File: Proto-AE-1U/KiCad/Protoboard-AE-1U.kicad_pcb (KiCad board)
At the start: 2 copper layers, 1 part

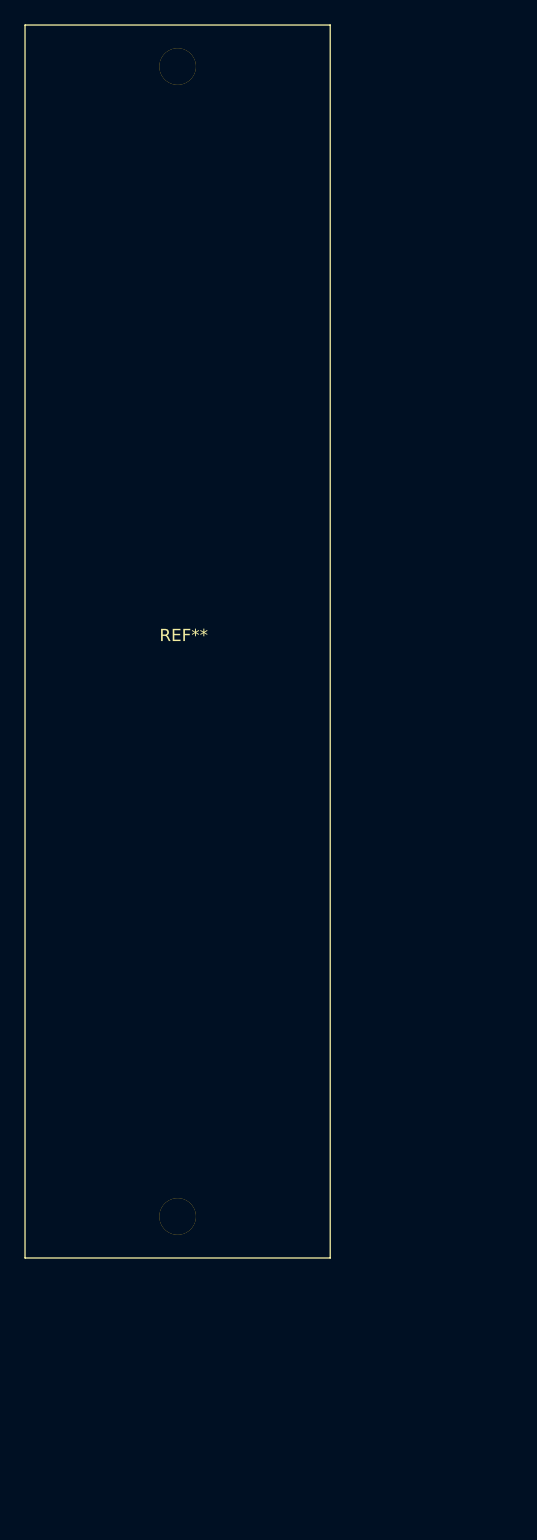
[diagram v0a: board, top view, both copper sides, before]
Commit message: created AE-1U-Protoboard
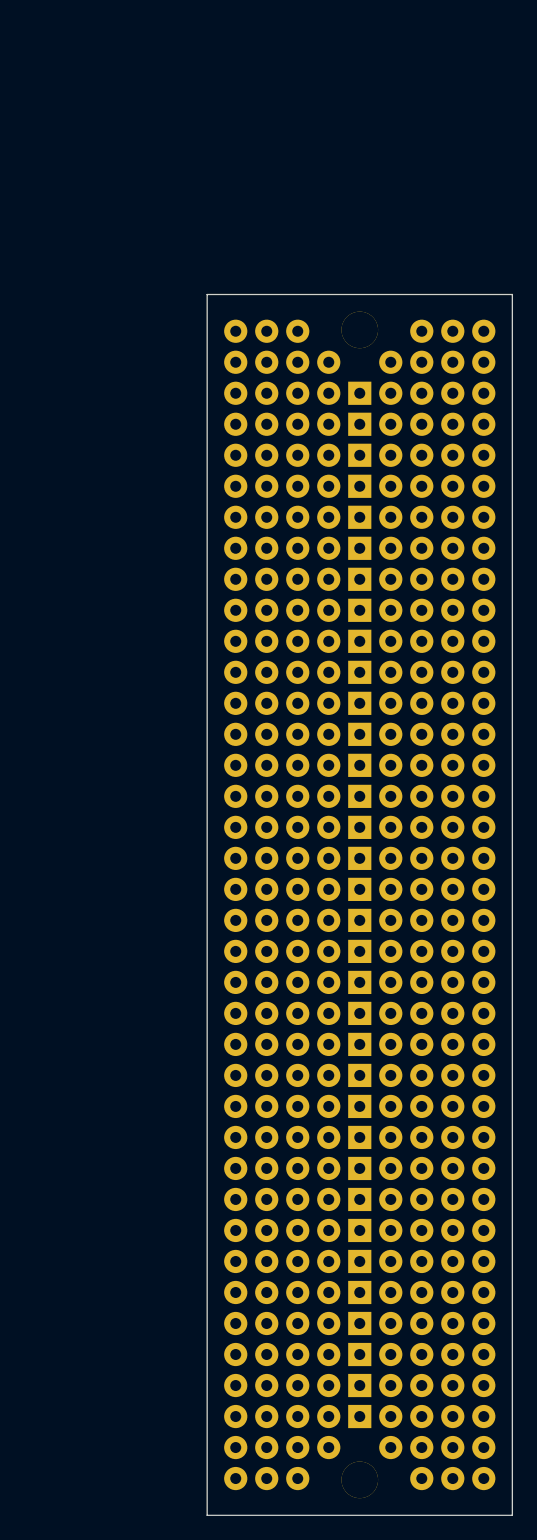
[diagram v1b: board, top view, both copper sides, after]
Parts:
- removed the REF** at (89.0, 131.0)
- added REF**: Pad, clectric-diy:Pad, F.Cu at (106.3, 72.9)
- added REF**: Pad, clectric-diy:Pad, F.Cu at (106.3, 105.9)
- added REF**: Pad, clectric-diy:Pad, F.Cu at (124.0, 65.2)
- added REF**: Pad, clectric-diy:Pad, F.Cu at (113.9, 121.1)
- added REF**: Pad, clectric-diy:Pad, F.Cu at (124.0, 80.5)
- added REF**: Pad, clectric-diy:Pad, F.Cu at (113.9, 88.1)
- added REF**: Pad, clectric-diy:Pad, F.Cu at (121.5, 149.1)
- added REF**: Pad, clectric-diy:Pad, F.Cu at (111.3, 131.3)
- added REF**: Pad, clectric-diy:Pad, F.Cu at (121.5, 133.8)
- added REF**: Pad, clectric-diy:Pad, F.Cu at (108.8, 62.7)
- added REF**: Pad, clectric-diy:Pad, F.Cu at (113.9, 113.5)
- added REF**: Pad, clectric-diy:Pad, F.Cu at (119.0, 113.5)
- added REF**: Pad, clectric-diy:Pad, F.Cu at (106.3, 138.9)
- added REF**: Pad, clectric-diy:Pad, F.Cu at (124.0, 75.4)
- added REF**: Pad, clectric-diy:Pad, F.Cu at (116.4, 123.7)
- added REF**: Pad, clectric-diy:Pad, F.Cu at (108.8, 108.4)
- added REF**: Pad, clectric-diy:Pad, F.Cu at (116.4, 67.8)
- added REF**: Pad, clectric-diy:Pad, F.Cu at (111.3, 80.5)
- added REF**: Pad, clectric-diy:Pad, F.Cu at (116.4, 111.0)
- added REF**: Pad, clectric-diy:Pad, F.Cu at (126.6, 75.4)
- added REF**: Pad, clectric-diy:Pad, F.Cu at (121.5, 116.0)
- added REF**: Pad, clectric-diy:Pad, F.Cu at (108.8, 116.0)
- added REF**: Pad, clectric-diy:Pad, F.Cu at (111.3, 136.4)
- added REF**: Pad, clectric-diy:Pad, F.Cu at (106.3, 95.7)
- added REF**: Pad, clectric-diy:Pad, F.Cu at (121.5, 126.2)
- added REF**: Pad, clectric-diy:Pad, F.Cu at (108.8, 149.1)
- added REF**: Pad, clectric-diy:Pad, F.Cu at (116.4, 121.1)
- added REF**: Pad, clectric-diy:Pad, F.Cu at (108.8, 136.4)
- added REF**: Pad, clectric-diy:Pad, F.Cu at (119.0, 60.2)
- added REF**: Pad, clectric-diy:Pad, F.Cu at (121.5, 67.8)
- added REF**: Pad, clectric-diy:Pad, F.Cu at (121.5, 90.6)
- added REF**: Pad, clectric-diy:Pad, F.Cu at (124.0, 105.9)
- added REF**: Pad, clectric-diy:Pad, F.Cu at (116.4, 80.5)
- added REF**: Pad, clectric-diy:Pad, F.Cu at (106.3, 108.4)
- added REF**: Pad, clectric-diy:Pad, F.Cu at (106.3, 85.6)
- added REF**: Pad, clectric-diy:Pad, F.Cu at (108.8, 90.6)
- added REF**: Pad, clectric-diy:Pad, F.Cu at (121.5, 98.3)
- added REF**: Pad, clectric-diy:Pad, F.Cu at (116.4, 75.4)
- added REF**: Pad, clectric-diy:Pad, F.Cu at (119.0, 103.3)
- added REF**: Pad, clectric-diy:Pad, F.Cu at (121.5, 108.4)
- added REF**: Pad, clectric-diy:Pad, F.Cu at (108.8, 133.8)
- added REF**: Pad, clectric-diy:Pad, F.Cu at (111.3, 77.9)
- added REF**: Pad, clectric-diy:Pad, F.Cu at (111.3, 100.8)
- added REF**: Pad, clectric-diy:Pad, F.Cu at (119.0, 105.9)
- added REF**: Pad, clectric-diy:Pad, F.Cu at (126.6, 121.1)
- added REF**: Pad, clectric-diy:Pad, F.Cu at (116.4, 118.6)
- added REF**: Pad, clectric-diy:Pad, F.Cu at (126.6, 136.4)
- added REF**: Pad, clectric-diy:Pad, F.Cu at (121.5, 141.4)
- added REF**: Pad, clectric-diy:Pad, F.Cu at (116.4, 116.0)
- added REF**: Pad, clectric-diy:Pad, F.Cu at (111.3, 123.7)
- added REF**: Pad, clectric-diy:Pad, F.Cu at (121.5, 121.1)
- added REF**: Pad, clectric-diy:Pad, F.Cu at (108.8, 111.0)
- added REF**: Pad, clectric-diy:Pad, F.Cu at (108.8, 88.1)
- added REF**: Pad, clectric-diy:Pad, F.Cu at (106.3, 116.0)
- added REF**: Pad, clectric-diy:Pad, F.Cu at (111.3, 65.2)
- added REF**: Pad, clectric-diy:Pad, F.Cu at (119.0, 75.4)
- added REF**: Pad, clectric-diy:Pad, F.Cu at (119.0, 146.5)
- added REF**: Pad, clectric-diy:Pad, F.Cu at (124.0, 100.8)
- added REF**: Pad, clectric-diy:Pad, F.Cu at (106.3, 80.5)
- added REF**: Pad, clectric-diy:Pad, F.Cu at (119.0, 90.6)
- added REF**: Pad, clectric-diy:Pad, F.Cu at (121.5, 144.0)
- added REF**: Pad, clectric-diy:Pad, F.Cu at (111.3, 108.4)
- added REF**: Pad, clectric-diy:Pad, F.Cu at (111.3, 72.9)
- added REF**: Pad, clectric-diy:Pad, F.Cu at (126.6, 144.0)
- added REF**: Pad, clectric-diy:Pad, F.Cu at (116.4, 133.8)
- added REF**: Pad, clectric-diy:Pad, F.Cu at (113.9, 133.8)
- added REF**: Pad, clectric-diy:Pad, F.Cu at (108.8, 93.2)
- added REF**: Pad, clectric-diy:Pad, F.Cu at (113.9, 141.4)
- added REF**: Pad, clectric-diy:Pad, F.Cu at (121.5, 72.9)
- added REF**: Pad, clectric-diy:Pad, F.Cu at (119.0, 133.8)
- added REF**: Pad, clectric-diy:Pad, F.Cu at (113.9, 123.7)
- added REF**: Pad, clectric-diy:Pad, F.Cu at (106.3, 90.6)
- added REF**: Pad, clectric-diy:Pad, F.Cu at (111.3, 55.1)
- added REF**: Pad, clectric-diy:Pad, F.Cu at (113.9, 93.2)
- added REF**: Pad, clectric-diy:Pad, F.Cu at (113.9, 67.8)
- added REF**: Pad, clectric-diy:Pad, F.Cu at (108.8, 146.5)
- added REF**: Pad, clectric-diy:Pad, F.Cu at (111.3, 118.6)
- added REF**: Pad, clectric-diy:Pad, F.Cu at (111.3, 85.6)
- added REF**: Pad, clectric-diy:Pad, F.Cu at (113.9, 103.3)
- added REF**: Pad, clectric-diy:Pad, F.Cu at (113.9, 77.9)
- added REF**: Pad, clectric-diy:Pad, F.Cu at (108.8, 131.3)
- added REF**: Pad, clectric-diy:Pad, F.Cu at (111.3, 98.3)
- added REF**: Pad, clectric-diy:Pad, F.Cu at (121.5, 83.0)
- added REF**: Pad, clectric-diy:Pad, F.Cu at (116.4, 65.2)
- added REF**: Pad, clectric-diy:Pad, F.Cu at (113.9, 100.8)
- added REF**: Pad, clectric-diy:Pad, F.Cu at (121.5, 85.6)
- added REF**: Pad, clectric-diy:Pad, F.Cu at (106.3, 111.0)
- added REF**: Pad, clectric-diy:Pad, F.Cu at (111.3, 93.2)
- added REF**: Pad, clectric-diy:Pad, F.Cu at (113.9, 98.3)
- added REF**: Pad, clectric-diy:Pad, F.Cu at (111.3, 95.7)
- added REF**: Pad, clectric-diy:Pad, F.Cu at (119.0, 144.0)
- added REF**: Pad, clectric-diy:Pad, F.Cu at (124.0, 126.2)
- added REF**: Pad, clectric-diy:Pad, F.Cu at (106.3, 126.2)
- added REF**: Pad, clectric-diy:Pad, F.Cu at (116.4, 136.4)
- added REF**: Pad, clectric-diy:Pad, F.Cu at (108.8, 123.7)
- added REF**: Pad, clectric-diy:Pad, F.Cu at (116.4, 131.3)
- added REF**: Pad, clectric-diy:Pad, F.Cu at (124.0, 116.0)
- added REF**: Pad, clectric-diy:Pad, F.Cu at (121.5, 128.7)
- added REF**: Pad, clectric-diy:Pad, F.Cu at (111.3, 126.2)
- added REF**: Pad, clectric-diy:Pad, F.Cu at (116.4, 93.2)
- added REF**: Pad, clectric-diy:Pad, F.Cu at (121.5, 55.1)
- added REF**: Pad, clectric-diy:Pad, F.Cu at (106.3, 100.8)
- added REF**: Pad, clectric-diy:Pad, F.Cu at (116.4, 144.0)
- added REF**: Pad, clectric-diy:Pad, F.Cu at (108.8, 72.9)
- added REF**: Pad, clectric-diy:Pad, F.Cu at (111.3, 90.6)
- added REF**: Pad, clectric-diy:Pad, F.Cu at (108.8, 98.3)
- added REF**: Pad, clectric-diy:Pad, F.Cu at (124.0, 118.6)
- added REF**: Pad, clectric-diy:Pad, F.Cu at (119.0, 126.2)
- added REF**: Pad, clectric-diy:Pad, F.Cu at (106.3, 123.7)
- added REF**: Pad, clectric-diy:Pad, F.Cu at (108.8, 77.9)
- added REF**: Pad, clectric-diy:Pad, F.Cu at (106.3, 55.1)
- added REF**: Pad, clectric-diy:Pad, F.Cu at (113.9, 90.6)
- added REF**: Pad, clectric-diy:Pad, F.Cu at (106.3, 144.0)
- added REF**: Pad, clectric-diy:Pad, F.Cu at (126.6, 62.7)
- added REF**: Pad, clectric-diy:Pad, F.Cu at (119.0, 93.2)
- added REF**: Pad, clectric-diy:Pad, F.Cu at (126.6, 65.2)
- added REF**: Pad, clectric-diy:Pad, F.Cu at (111.3, 67.8)
- added REF**: Pad, clectric-diy:Pad, F.Cu at (108.8, 126.2)
- added REF**: Pad, clectric-diy:Pad, F.Cu at (124.0, 77.9)
- added REF**: Pad, clectric-diy:Pad, F.Cu at (106.3, 118.6)
- added REF**: Pad, clectric-diy:Pad, F.Cu at (108.8, 128.7)
- added REF**: Pad, clectric-diy:Pad, F.Cu at (126.6, 77.9)
- added REF**: Pad, clectric-diy:Pad, F.Cu at (126.6, 141.4)
- added REF**: Pad, clectric-diy:Pad, F.Cu at (108.8, 60.2)
- added REF**: Pad, clectric-diy:Pad, F.Cu at (119.0, 80.5)
- added REF**: Pad, clectric-diy:Pad, F.Cu at (124.0, 57.6)
- added REF**: Pad, clectric-diy:Pad, F.Cu at (116.4, 88.1)
- added REF**: Pad, clectric-diy:Pad, F.Cu at (119.0, 108.4)
- added REF**: Pad, clectric-diy:Pad, F.Cu at (119.0, 138.9)
- added REF**: Pad, clectric-diy:Pad, F.Cu at (119.0, 65.2)
- added REF**: Pad, clectric-diy:Pad, F.Cu at (126.6, 146.5)
- added REF**: Pad, clectric-diy:Pad, F.Cu at (126.6, 118.6)
- added REF**: Pad, clectric-diy:Pad, F.Cu at (111.3, 138.9)
- added REF**: Pad, clectric-diy:Pad, F.Cu at (111.3, 105.9)
- added REF**: Pad, clectric-diy:Pad, F.Cu at (111.3, 149.1)
- added REF**: Pad, clectric-diy:Pad, F.Cu at (106.3, 77.9)
- added REF**: Pad, clectric-diy:Pad, F.Cu at (113.9, 118.6)
- added REF**: Pad, clectric-diy:Pad, F.Cu at (121.5, 95.7)
- added REF**: Pad, clectric-diy:Pad, F.Cu at (113.9, 128.7)
- added REF**: Pad, clectric-diy:Pad, F.Cu at (108.8, 67.8)
- added REF**: Pad, clectric-diy:Pad, F.Cu at (121.5, 93.2)
- added REF**: Pad, clectric-diy:Pad, F.Cu at (113.9, 144.0)
- added REF**: Pad, clectric-diy:Pad, F.Cu at (119.0, 83.0)
- added REF**: Pad, clectric-diy:Pad, F.Cu at (106.3, 103.3)
- added REF**: Pad, clectric-diy:Pad, F.Cu at (126.6, 133.8)
- added REF**: Pad, clectric-diy:Pad, F.Cu at (119.0, 95.7)
- added REF**: Pad, clectric-diy:Pad, F.Cu at (106.3, 65.2)
- added REF**: Pad, clectric-diy:Pad, F.Cu at (111.3, 83.0)
- added REF**: Pad, clectric-diy:Pad, F.Cu at (116.4, 138.9)
- added REF**: Pad, clectric-diy:Pad, F.Cu at (126.6, 131.3)
- added REF**: Pad, clectric-diy:Pad, F.Cu at (121.5, 88.1)
- added REF**: Pad, clectric-diy:Pad, F.Cu at (121.5, 123.7)
- added REF**: Pad, clectric-diy:Pad, F.Cu at (121.5, 138.9)
- added REF**: Pad, clectric-diy:Pad, F.Cu at (126.6, 111.0)
- added REF**: Pad, clectric-diy:Pad, F.Cu at (108.8, 100.8)
- added REF**: Pad, clectric-diy:Pad, F.Cu at (113.9, 72.9)
- added REF**: Pad, clectric-diy:Pad, F.Cu at (126.6, 126.2)
- added REF**: Pad, clectric-diy:Pad, F.Cu at (108.8, 118.6)
- added REF**: Pad, clectric-diy:Pad, F.Cu at (126.6, 98.3)
- added REF**: Pad, clectric-diy:Pad, F.Cu at (124.0, 108.4)
- added REF**: Pad, clectric-diy:Pad, F.Cu at (111.3, 133.8)
- added REF**: Pad, clectric-diy:Pad, F.Cu at (124.0, 83.0)
- added REF**: Pad, clectric-diy:Pad, F.Cu at (108.8, 113.5)
- added REF**: Pad, clectric-diy:Pad, F.Cu at (108.8, 80.5)
- added REF**: Pad, clectric-diy:Pad, F.Cu at (119.0, 128.7)
- added REF**: Pad, clectric-diy:Pad, F.Cu at (119.0, 70.3)
- added REF**: Pad, clectric-diy:Pad, F.Cu at (126.6, 60.2)
- added REF**: Pad, clectric-diy:Pad, F.Cu at (113.9, 85.6)
- added REF**: Pad, clectric-diy:Pad, F.Cu at (106.3, 88.1)
- added REF**: Pad, clectric-diy:Pad, F.Cu at (119.0, 88.1)
- added REF**: Pad, clectric-diy:Pad, F.Cu at (113.9, 70.3)
- added REF**: Pad, clectric-diy:Pad, F.Cu at (124.0, 138.9)
- added REF**: Pad, clectric-diy:Pad, F.Cu at (106.3, 141.4)
- added REF**: Pad, clectric-diy:Pad, F.Cu at (124.0, 103.3)
- added REF**: Pad, clectric-diy:Pad, F.Cu at (121.5, 111.0)
- added REF**: Pad, clectric-diy:Pad, F.Cu at (108.8, 141.4)
- added REF**: Pad, clectric-diy:Pad, F.Cu at (119.0, 57.6)
- added REF**: Pad, clectric-diy:Pad, F.Cu at (126.6, 100.8)
- added REF**: Pad, clectric-diy:Pad, F.Cu at (116.4, 90.6)
- added REF**: Pad, clectric-diy:Pad, F.Cu at (124.0, 98.3)
- added REF**: Pad, clectric-diy:Pad, F.Cu at (126.6, 138.9)
- added REF**: Pad, clectric-diy:Pad, F.Cu at (124.0, 88.1)
- added REF**: Pad, clectric-diy:Pad, F.Cu at (108.8, 95.7)
- added REF**: Pad, clectric-diy:Pad, F.Cu at (124.0, 67.8)
- added REF**: Pad, clectric-diy:Pad, F.Cu at (119.0, 98.3)
- added REF**: Pad, clectric-diy:Pad, F.Cu at (111.3, 111.0)
- added REF**: Pad, clectric-diy:Pad, F.Cu at (126.6, 72.9)
- added REF**: Pad, clectric-diy:Pad, F.Cu at (108.8, 144.0)
- added REF**: Pad, clectric-diy:Pad, F.Cu at (116.4, 154.1)
- added REF**: Pad, clectric-diy:Pad, F.Cu at (124.0, 149.1)
- added REF**: Pad, clectric-diy:Pad, F.Cu at (124.0, 136.4)
- added REF**: Pad, clectric-diy:Pad, F.Cu at (126.6, 108.4)
- added REF**: Pad, clectric-diy:Pad, F.Cu at (106.3, 149.1)
- added REF**: Pad, clectric-diy:Pad, F.Cu at (121.5, 146.5)
- added REF**: Pad, clectric-diy:Pad, F.Cu at (116.4, 113.5)
- added REF**: Pad, clectric-diy:Pad, F.Cu at (124.0, 90.6)
- added REF**: Pad, clectric-diy:Pad, F.Cu at (126.6, 90.6)
- added REF**: Pad, clectric-diy:Pad, F.Cu at (126.6, 80.5)
- added REF**: Pad, clectric-diy:Pad, F.Cu at (119.0, 121.1)
- added REF**: Pad, clectric-diy:Pad, F.Cu at (126.6, 105.9)
- added REF**: Pad, clectric-diy:Pad, F.Cu at (106.3, 128.7)
- added REF**: Pad, clectric-diy:Pad, F.Cu at (111.3, 70.3)
- added REF**: Pad, clectric-diy:Pad, F.Cu at (111.3, 141.4)
- added REF**: Pad, clectric-diy:Pad, F.Cu at (116.4, 77.9)
- added REF**: Pad, clectric-diy:Pad, F.Cu at (124.0, 141.4)
- added REF**: Pad, clectric-diy:Pad, F.Cu at (126.6, 93.2)
- added REF**: Pad, clectric-diy:Pad, F.Cu at (126.6, 88.1)
- added REF**: Pad, clectric-diy:Pad, F.Cu at (106.3, 60.2)
- added REF**: Pad, clectric-diy:Pad, F.Cu at (126.6, 128.7)
- added REF**: Pad, clectric-diy:Pad, F.Cu at (119.0, 118.6)
- added REF**: Pad, clectric-diy:Pad, F.Cu at (119.0, 72.9)
- added REF**: Pad, clectric-diy:Pad, F.Cu at (121.5, 57.6)
- added REF**: Pad, clectric-diy:Pad, F.Cu at (106.3, 67.8)
- added REF**: Pad, clectric-diy:Pad, F.Cu at (116.4, 83.0)
- added REF**: Pad, clectric-diy:Pad, F.Cu at (126.6, 95.7)
- added REF**: Pad, clectric-diy:Pad, F.Cu at (126.6, 113.5)
- added REF**: Pad, clectric-diy:Pad, F.Cu at (124.0, 144.0)
- added REF**: Pad, clectric-diy:Pad, F.Cu at (121.5, 103.3)
- added REF**: Pad, clectric-diy:Pad, F.Cu at (124.0, 128.7)
- added REF**: Pad, clectric-diy:Pad, F.Cu at (121.5, 113.5)
- added REF**: Pad, clectric-diy:Pad, F.Cu at (116.4, 62.7)
- added REF**: Pad, clectric-diy:Pad, F.Cu at (126.6, 55.1)
- added REF**: Pad, clectric-diy:Pad, F.Cu at (113.9, 80.5)
- added REF**: Pad, clectric-diy:Pad, F.Cu at (126.6, 67.8)
- added REF**: Pad, clectric-diy:Pad, F.Cu at (108.8, 121.1)
- added REF**: Pad, clectric-diy:Pad, F.Cu at (111.3, 88.1)
- added REF**: Pad, clectric-diy:Pad, F.Cu at (124.0, 70.3)
- added REF**: Pad, clectric-diy:Pad, F.Cu at (124.0, 72.9)
- added REF**: Pad, clectric-diy:Pad, F.Cu at (126.6, 83.0)
- added REF**: Pad, clectric-diy:Pad, F.Cu at (111.3, 144.0)
- added REF**: Pad, clectric-diy:Pad, F.Cu at (121.5, 136.4)
- added REF**: Pad, clectric-diy:Pad, F.Cu at (111.3, 128.7)
- added REF**: Pad, clectric-diy:Pad, F.Cu at (111.3, 57.6)
- added REF**: Pad, clectric-diy:Pad, F.Cu at (124.0, 62.7)
- added REF**: Pad, clectric-diy:Pad, F.Cu at (119.0, 116.0)
- added REF**: Pad, clectric-diy:Pad, F.Cu at (119.0, 62.7)
- added REF**: Pad, clectric-diy:Pad, F.Cu at (124.0, 113.5)
- added REF**: Pad, clectric-diy:Pad, F.Cu at (106.3, 98.3)
- added REF**: Pad, clectric-diy:Pad, F.Cu at (124.0, 85.6)
- added REF**: Pad, clectric-diy:Pad, F.Cu at (106.3, 113.5)
- added REF**: Pad, clectric-diy:Pad, F.Cu at (119.0, 111.0)
- added REF**: Pad, clectric-diy:Pad, F.Cu at (113.9, 95.7)
- added REF**: Pad, clectric-diy:Pad, F.Cu at (126.6, 85.6)
- added REF**: Pad, clectric-diy:Pad, F.Cu at (124.0, 131.3)
- added REF**: Pad, clectric-diy:Pad, F.Cu at (119.0, 67.8)
- added REF**: Pad, clectric-diy:Pad, F.Cu at (119.0, 77.9)
- added REF**: Pad, clectric-diy:Pad, F.Cu at (113.9, 136.4)
- added REF**: Pad, clectric-diy:Pad, F.Cu at (119.0, 85.6)
- added REF**: Pad, clectric-diy:Pad, F.Cu at (116.4, 126.2)
- added REF**: Pad, clectric-diy:Pad, F.Cu at (111.3, 116.0)
- added REF**: Pad, clectric-diy:Pad, F.Cu at (113.9, 62.7)
- added REF**: Pad, clectric-diy:Pad, F.Cu at (116.4, 85.6)
- added REF**: Pad, clectric-diy:Pad, F.Cu at (111.3, 146.5)
- added REF**: Pad, clectric-diy:Pad, F.Cu at (119.0, 100.8)
- added REF**: Pad, clectric-diy:Pad, F.Cu at (124.0, 93.2)
- added REF**: Pad, clectric-diy:Pad, F.Cu at (111.3, 113.5)
- added REF**: Pad, clectric-diy:Pad, F.Cu at (108.8, 55.1)
- added REF**: Pad, clectric-diy:Pad, F.Cu at (113.9, 131.3)
- added REF**: Pad, clectric-diy:Pad, F.Cu at (116.4, 105.9)
- added REF**: Pad, clectric-diy:Pad, F.Cu at (111.3, 75.4)
- added REF**: Pad, clectric-diy:Pad, F.Cu at (113.9, 75.4)
- added REF**: Pad, clectric-diy:Pad, F.Cu at (121.5, 65.2)
- added REF**: Pad, clectric-diy:Pad, F.Cu at (108.8, 83.0)
- added REF**: Pad, clectric-diy:Pad, F.Cu at (108.8, 57.6)
- added REF**: Pad, clectric-diy:Pad, F.Cu at (119.0, 131.3)
- added REF**: Pad, clectric-diy:Pad, F.Cu at (124.0, 55.1)
- added REF**: Pad, clectric-diy:Pad, F.Cu at (108.8, 138.9)
- added REF**: Pad, clectric-diy:Pad, F.Cu at (124.0, 60.2)
- added REF**: Pad, clectric-diy:Pad, F.Cu at (106.3, 83.0)
- added REF**: Pad, clectric-diy:Pad, F.Cu at (106.3, 93.2)
- added REF**: Pad, clectric-diy:Pad, F.Cu at (113.9, 105.9)
- added REF**: Pad, clectric-diy:Pad, F.Cu at (124.0, 95.7)
- added REF**: Pad, clectric-diy:Pad, F.Cu at (121.5, 77.9)
- added REF**: Pad, clectric-diy:Pad, F.Cu at (113.9, 57.6)
- added REF**: Pad, clectric-diy:Pad, F.Cu at (113.9, 108.4)
- added REF**: Pad, clectric-diy:Pad, F.Cu at (116.4, 60.2)
- added REF**: Pad, clectric-diy:Pad, F.Cu at (106.3, 62.7)
- added REF**: Pad, clectric-diy:Pad, F.Cu at (126.6, 103.3)
- added REF**: Pad, clectric-diy:Pad, F.Cu at (116.4, 70.3)
- added REF**: Pad, clectric-diy:Pad, F.Cu at (108.8, 75.4)
- added REF**: Pad, clectric-diy:Pad, F.Cu at (113.9, 111.0)
- added REF**: Pad, clectric-diy:Pad, F.Cu at (106.3, 146.5)
- added REF**: Pad, clectric-diy:Pad, F.Cu at (119.0, 136.4)
- added REF**: Pad, clectric-diy:Pad, F.Cu at (116.4, 72.9)
- added REF**: Pad, clectric-diy:Pad, F.Cu at (106.3, 136.4)
- added REF**: Pad, clectric-diy:Pad, F.Cu at (116.4, 95.7)
- added REF**: Pad, clectric-diy:Pad, F.Cu at (116.4, 55.0)
- added REF**: Pad, clectric-diy:Pad, F.Cu at (116.4, 108.4)
- added REF**: Pad, clectric-diy:Pad, F.Cu at (113.9, 138.9)
- added REF**: Pad, clectric-diy:Pad, F.Cu at (106.3, 131.3)
- added REF**: Pad, clectric-diy:Pad, F.Cu at (106.3, 70.3)
- added REF**: Pad, clectric-diy:Pad, F.Cu at (108.8, 70.3)
- added REF**: Pad, clectric-diy:Pad, F.Cu at (116.4, 128.7)
- added REF**: Pad, clectric-diy:Pad, F.Cu at (126.6, 149.1)
- added REF**: Pad, clectric-diy:Pad, F.Cu at (116.4, 100.8)
- added REF**: Pad, clectric-diy:Pad, F.Cu at (119.0, 123.7)
- added REF**: Pad, clectric-diy:Pad, F.Cu at (106.3, 133.8)
- added REF**: Pad, clectric-diy:Pad, F.Cu at (106.3, 121.1)
- added REF**: Pad, clectric-diy:Pad, F.Cu at (108.8, 105.9)
- added REF**: Pad, clectric-diy:Pad, F.Cu at (108.8, 85.6)
- added REF**: Pad, clectric-diy:Pad, F.Cu at (126.6, 123.7)
- added REF**: Pad, clectric-diy:Pad, F.Cu at (113.9, 65.2)
- added REF**: Pad, clectric-diy:Pad, F.Cu at (106.3, 57.6)
- added REF**: Pad, clectric-diy:Pad, F.Cu at (121.5, 118.6)
- added REF**: Pad, clectric-diy:Pad, F.Cu at (121.5, 131.3)
- added REF**: Pad, clectric-diy:Pad, F.Cu at (108.8, 103.3)
- added REF**: Pad, clectric-diy:Pad, F.Cu at (126.6, 57.6)
- added REF**: Pad, clectric-diy:Pad, F.Cu at (121.5, 62.7)
- added REF**: Pad, clectric-diy:Pad, F.Cu at (119.0, 141.4)
- added REF**: Pad, clectric-diy:Pad, F.Cu at (124.0, 123.7)
- added REF**: Pad, clectric-diy:Pad, F.Cu at (106.3, 75.4)
- added REF**: Pad, clectric-diy:Pad, F.Cu at (111.3, 103.3)
- added REF**: Pad, clectric-diy:Pad, F.Cu at (124.0, 121.1)
- added REF**: Pad, clectric-diy:Pad, F.Cu at (113.9, 116.0)
- added REF**: Pad, clectric-diy:Pad, F.Cu at (116.4, 98.3)
- added REF**: Pad, clectric-diy:Pad, F.Cu at (113.9, 126.2)
- added REF**: Pad, clectric-diy:Pad, F.Cu at (121.5, 75.4)
- added REF**: Pad, clectric-diy:Pad, F.Cu at (116.4, 103.3)
- added REF**: Pad, clectric-diy:Pad, F.Cu at (108.8, 65.2)
- added REF**: Pad, clectric-diy:Pad, F.Cu at (111.3, 60.2)
- added REF**: Pad, clectric-diy:Pad, F.Cu at (121.5, 80.5)
- added REF**: Pad, clectric-diy:Pad, F.Cu at (126.6, 116.0)
- added REF**: Pad, clectric-diy:Pad, F.Cu at (111.3, 62.7)
- added REF**: Pad, clectric-diy:Pad, F.Cu at (121.5, 70.3)
- added REF**: Pad, clectric-diy:Pad, F.Cu at (121.5, 100.8)
- added REF**: Pad, clectric-diy:Pad, F.Cu at (124.0, 146.5)
- added REF**: Pad, clectric-diy:Pad, F.Cu at (113.9, 60.2)
- added REF**: Pad, clectric-diy:Pad, F.Cu at (126.6, 70.3)
- added REF**: Pad, clectric-diy:Pad, F.Cu at (116.4, 141.4)
- added REF**: Pad, clectric-diy:Pad, F.Cu at (113.9, 83.0)
- added REF**: Pad, clectric-diy:Pad, F.Cu at (124.0, 133.8)
- added REF**: Pad, clectric-diy:Pad, F.Cu at (113.9, 146.5)
- added REF**: Pad, clectric-diy:Pad, F.Cu at (121.5, 105.9)
- added REF**: Pad, clectric-diy:Pad, F.Cu at (121.5, 60.2)
- added REF**: Pad, clectric-diy:Pad, F.Cu at (124.0, 111.0)
- added REF**: Pad, clectric-diy:Pad, F.Cu at (111.3, 121.1)
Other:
- board outline added: 25 x 100 mm
- copper layers 2 -> 4
